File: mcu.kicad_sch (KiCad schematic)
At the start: 22 parts, among them J1 USB_C_Receptacle_USB2.0_16P, SW1 SW_Push, U1 ESP32-S3-MINI-1U, U4 HLK-10M05, U6 TLV62569DBV

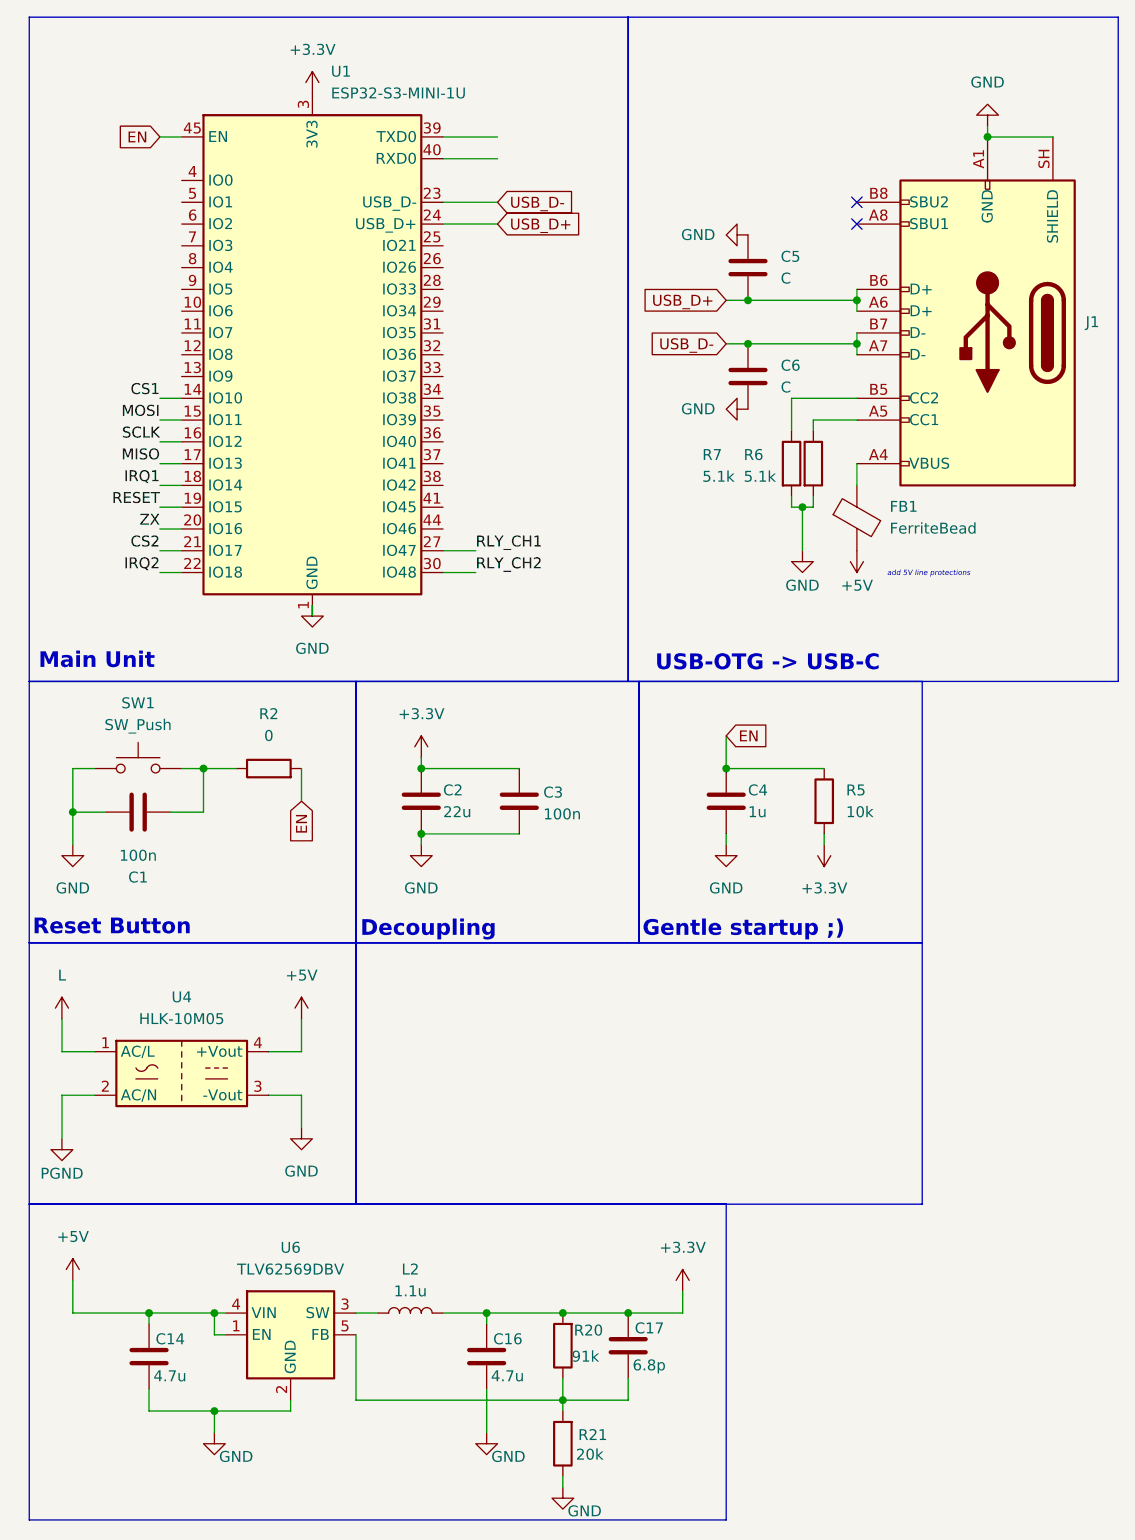
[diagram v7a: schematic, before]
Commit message: moved LDO to mcu sheet
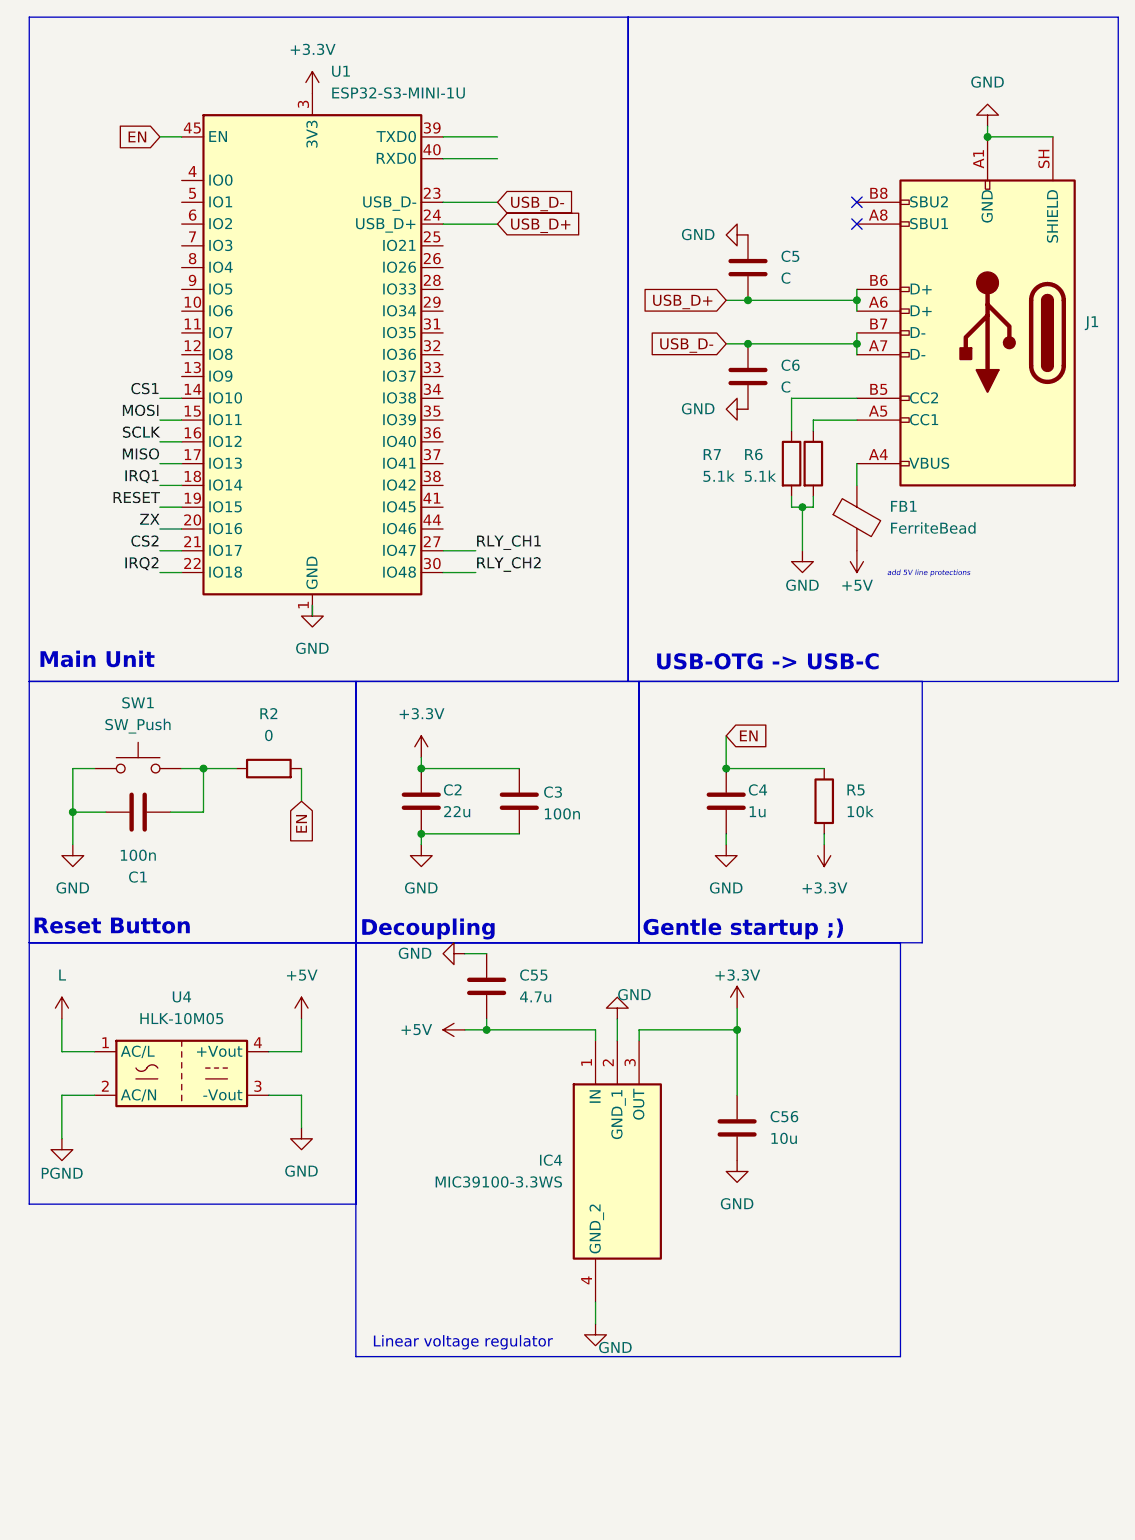
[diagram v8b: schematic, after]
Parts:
- removed C14, C16: 4.7u, symbol Device:C
- removed C17: 6.8p, symbol Device:C
- removed L2: 1.1u, symbol Device:L
- removed R20: 91k, symbol Device:R
- removed R21: 20k, symbol Device:R
- removed U6: TLV62569DBV, Package_TO_SOT_SMD:SOT-23-5, symbol Regulator_Switching:TLV62569DBV
- added C55: 4.7u, Capacitor_SMD:C_0805_2012Metric, symbol Device:C
- added C56: 10u, Capacitor_SMD:C_0805_2012Metric, symbol Device:C
- added IC4: MIC39100-3.3WS, SOT230P700X180-4N, symbol SamacSys_Parts:MIC39100-3.3WS
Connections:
- net +3.3V: now also C56.1, IC4.3 (OUT)
- net +5V: now also C55.2, IC4.1 (IN)
- net GND: now also C55.1, C56.2, IC4.2 (GND_1), IC4.4 (GND_2)
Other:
- note added: "Linear voltage regulator"
